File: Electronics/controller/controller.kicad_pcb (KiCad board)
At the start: 2 copper layers, 73.7 x 61 mm, 27 parts, among them P1 POWER, P2 PANEL_1, P3 PANEL_2, P4 DIAL, P5 SWITCH, P6 LED_DISPLAY, Q1 BUZ11, U1 LM317T, U2 74HC595, U3 Arduino_Pro_Micro

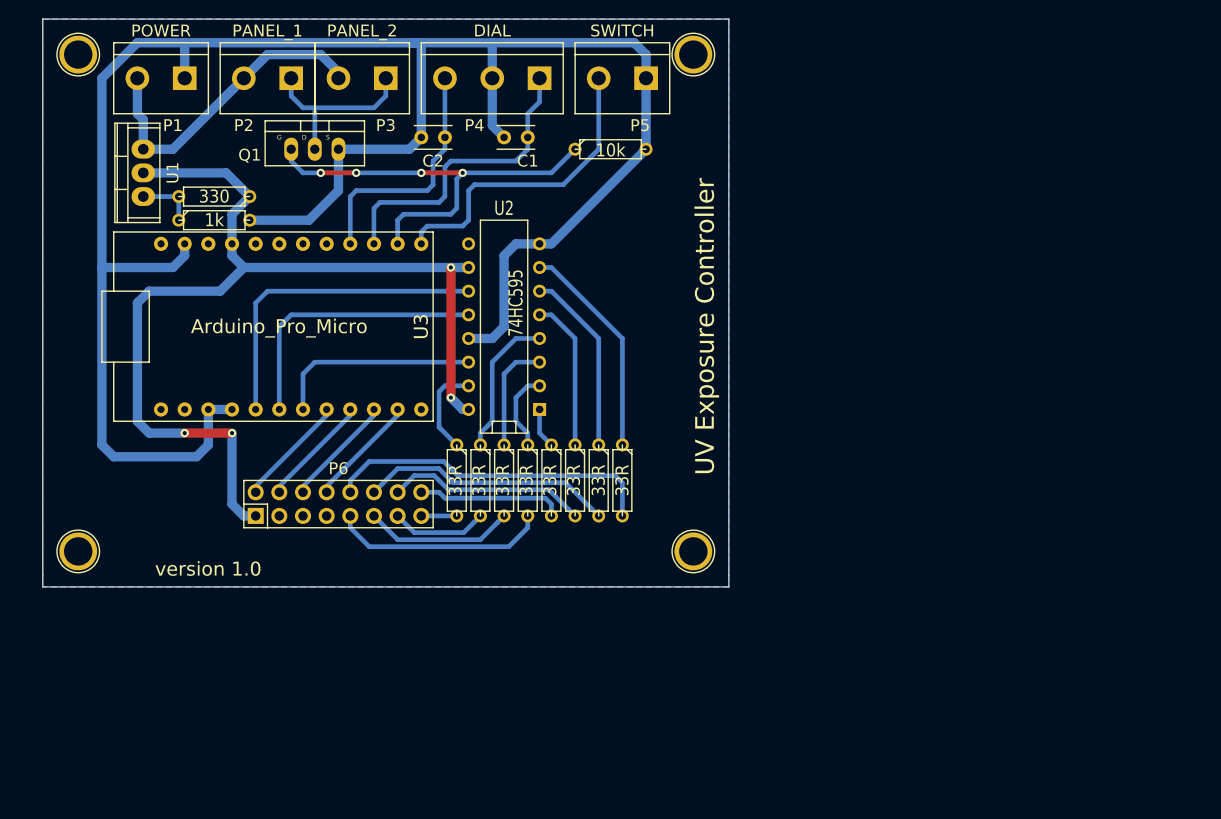
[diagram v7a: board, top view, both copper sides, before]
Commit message: Putting the display onto the board directly.
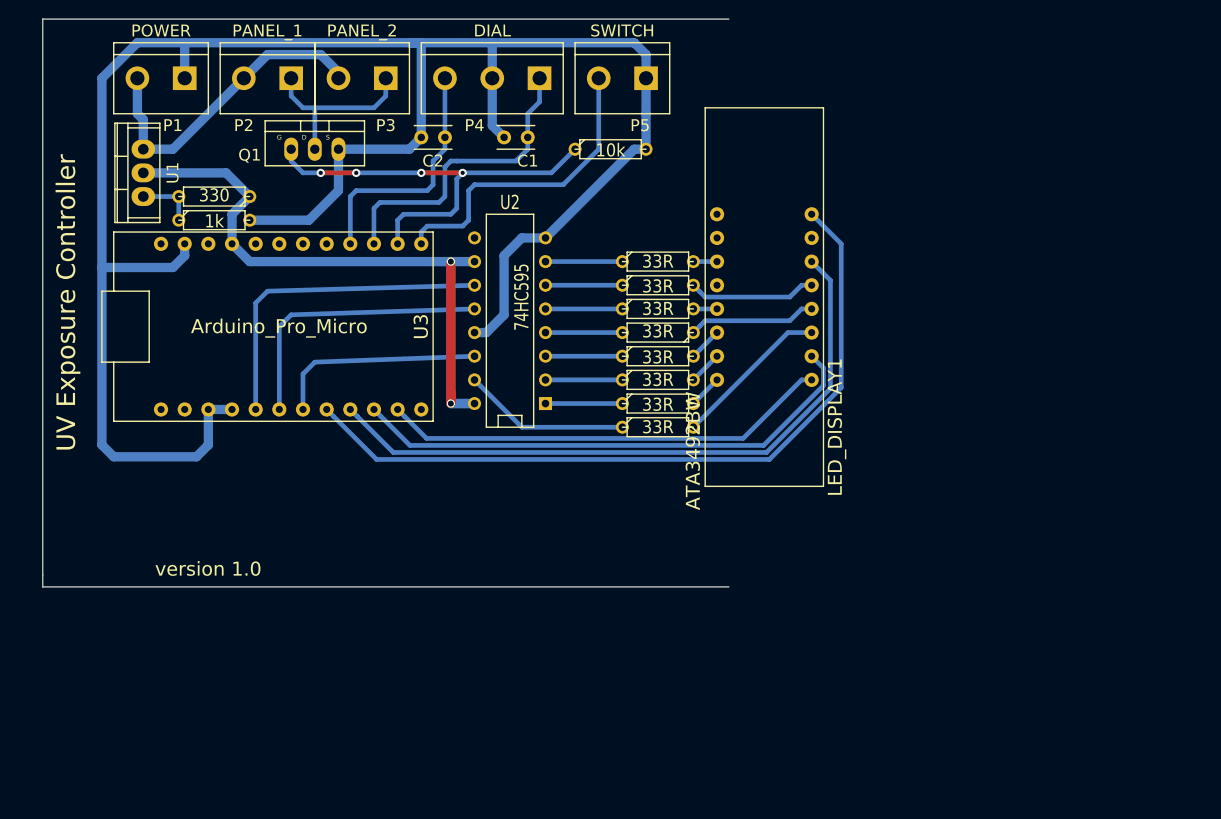
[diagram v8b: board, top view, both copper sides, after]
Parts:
- removed 1PIN (x4): P***, Connect:1pin
- removed P6: LED_DISPLAY, Pin_Headers:Pin_Header_Straight_2x08
- added LED_DISPLAY1: ATA3492BW, Cylindric:4_Digit-7_Segment_LED-ATA3492BW, F.Cu at (181.6, 81.9)
- Q1: value BUZ11 -> FET
- R10: value 330 -> 33R
- R11: value 1k -> 33R
- R2: value 33R -> 1k
- R3: value 33R -> 330
- R4: value 33R -> 10k
- R9: value 10k -> 33R
- moved R11 50.6 mm to (170.2, 90.8)
- moved R10 48.1 mm to (170.2, 78.1), turned to 0 degrees
- moved R3 43.6 mm to (122.6, 71.1), turned to 180 degrees
- moved R2 40.0 mm to (122.6, 73.7), turned to 0 degrees
- moved R4 36.7 mm to (165.1, 66.0), turned to 0 degrees
- moved R1 26.8 mm to (170.2, 85.7), turned to 180 degrees
- moved R7 19.5 mm to (170.2, 83.2), turned to 0 degrees
- moved R5 17.6 mm to (170.2, 88.3), turned to 0 degrees
- moved R9 15.5 mm to (170.2, 80.6)
- moved R6 12.1 mm to (170.2, 93.3), turned to 0 degrees
- moved R8 6.87 mm to (170.2, 95.9), turned to 0 degrees
- moved U2 0.90 mm to (154.3, 84.5)
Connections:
- R1 pad 1: /COL -> Net-(LED_DISPLAY1-Pad4)
- R1 pad 2: Net-(P6-Pad15) -> /COL
- R10 pad 1: VCC -> /F
- R10 pad 2: Net-(R10-Pad2) -> Net-(LED_DISPLAY1-Pad11)
- R11 pad 1: Net-(R10-Pad2) -> /G
- R11 pad 2: GND -> Net-(LED_DISPLAY1-Pad15)
- R2 pad 1: /D -> Net-(R2-Pad1)
- R2 pad 2: Net-(P6-Pad13) -> GND
- R3 pad 1: /C -> VCC
- R3 pad 2: Net-(P6-Pad11) -> Net-(R2-Pad1)
- R4 pad 1: /B -> /D16
- R4 pad 2: Net-(P6-Pad9) -> GND
- R6 pad 1: /E -> /B
- R7 pad 1: /F -> /C
- R8 pad 1: /G -> /D
- R9 pad 1: /D16 -> /E
- R9 pad 2: GND -> Net-(LED_DISPLAY1-Pad5)
- U1 pad 1: Net-(R10-Pad2) -> Net-(R2-Pad1)
- U2 pad 1: /A -> /B
- U2 pad 15: /COL -> /D
- U2 pad 2: /B -> /G
- U2 pad 3: /C -> /A
- U2 pad 4: /D -> /COL
- U2 pad 5: /E -> /C
- U2 pad 6: /F -> /E
- U2 pad 7: /G -> /F
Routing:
- net /D8: track 12.0 -> 80.6 mm
- net /D7: track 12.0 -> 70.8 mm
- net /D6: track 12.0 -> 56.2 mm
- net VCC: track 109.0 -> 66.1 mm, vias 4 -> 2
- net /D5: track 12.0 -> 48.3 mm
- net Net-(LED_DISPLAY1-Pad13): track 27.7 -> 2.54 mm
- net Net-(P6-Pad9): track 23.3 -> 0.00 mm
- net Net-(LED_DISPLAY1-Pad3): track 35.8 -> 16.9 mm
- net Net-(LED_DISPLAY1-Pad16): track 21.6 -> 3.59 mm
- net Net-(P6-Pad11): track 16.1 -> 0.00 mm
- net /G: track 23.5 -> 8.25 mm
- net Net-(LED_DISPLAY1-Pad4): track 0.00 -> 13.8 mm
- net Net-(LED_DISPLAY1-Pad5): track 0.00 -> 13.7 mm
- net Net-(LED_DISPLAY1-Pad14): track 15.8 -> 3.59 mm
- net /F: track 19.9 -> 8.25 mm
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- removed copper zone on B.Cu, net GND
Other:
- outline, holes or cut-outs redrawn
